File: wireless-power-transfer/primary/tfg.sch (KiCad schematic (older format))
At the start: 30 parts, among them J1 CONN_01X06, J2 Screw_Terminal_1x02, J3 BARREL_JACK, Q1 IRLB8721PBF, Q2 IRLB8721PBF, Q3 IRLB8721PBF, Q4 IRLB8721PBF, U1 PIC18F45K20-I/PT, U2 IR2110, U3 IR2110, U4 R-78E15, U5 R-78E3.3, U6 XBEE_Wi-Fi

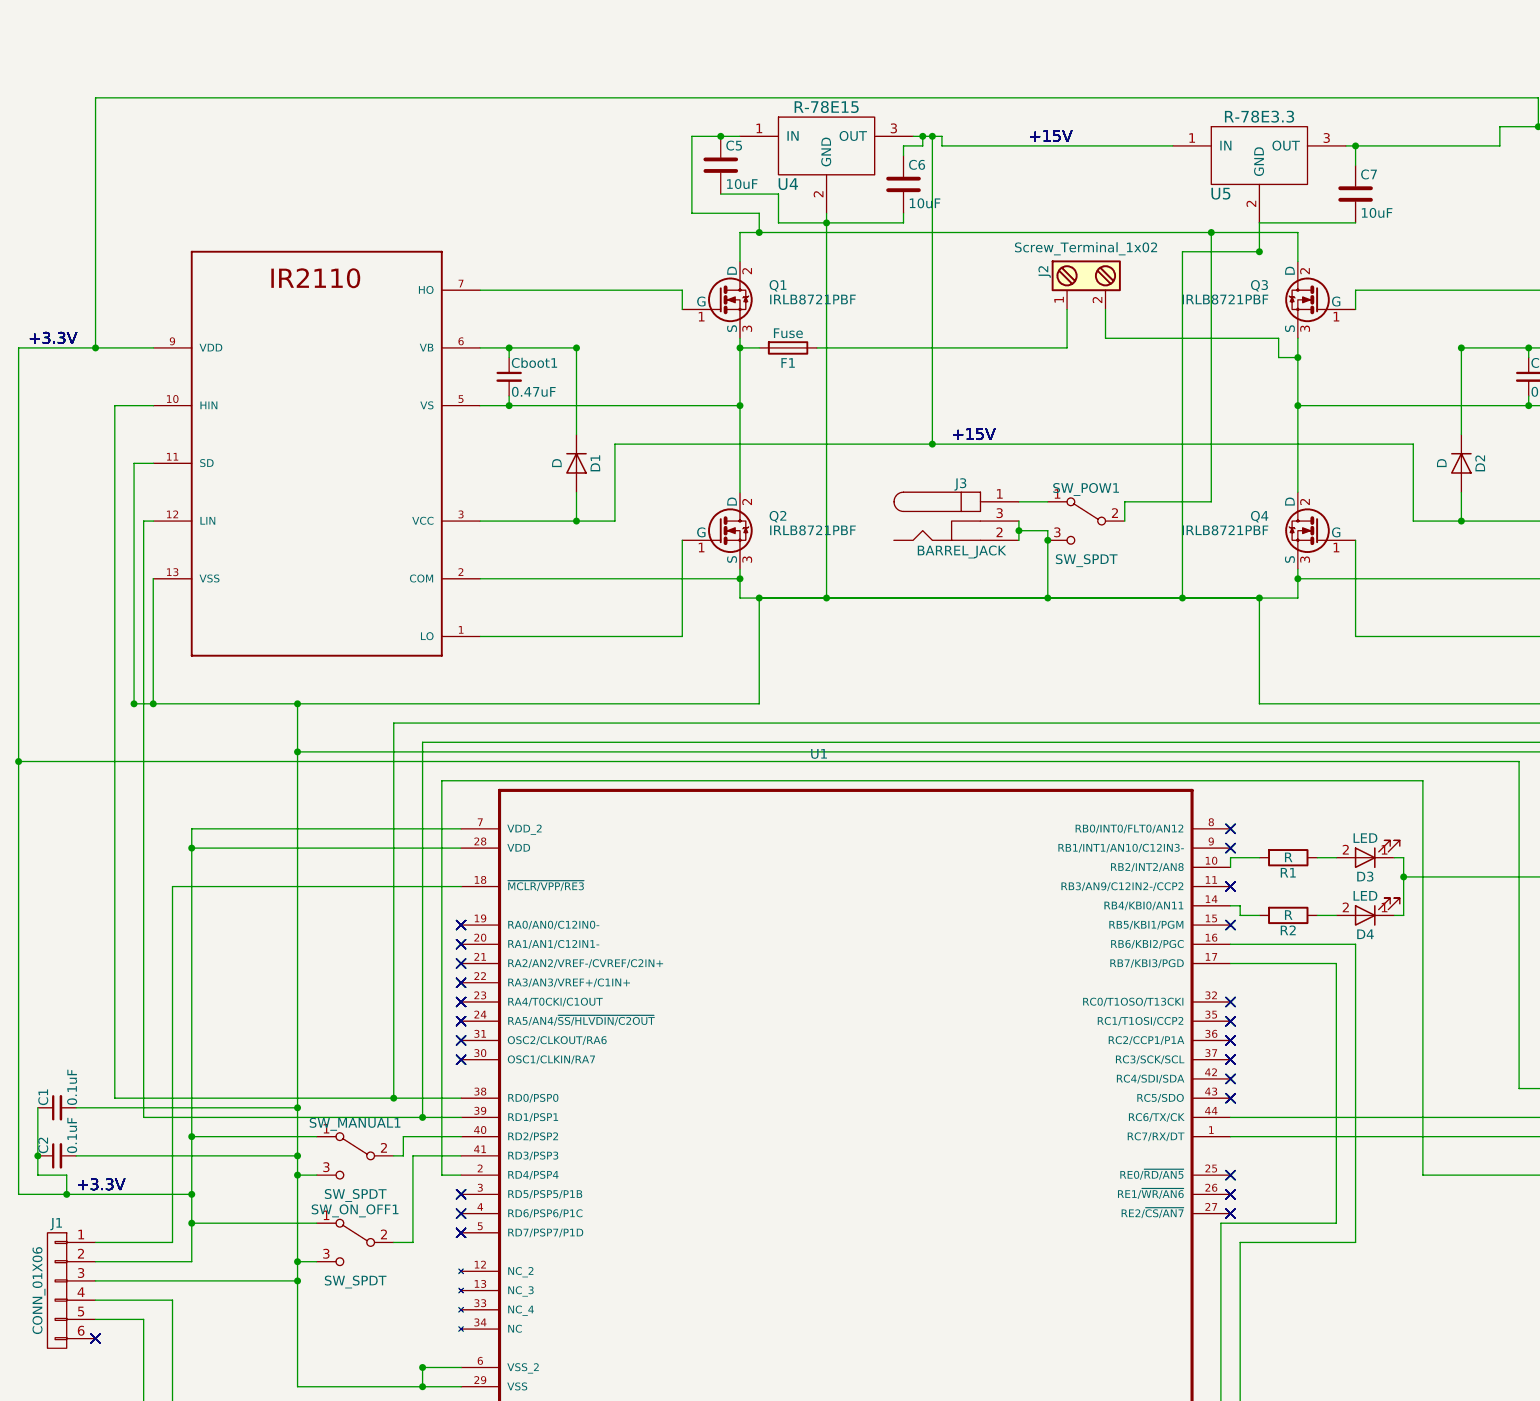
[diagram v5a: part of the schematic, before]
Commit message: Added resistor between pins 1 and 2 of the PicKit connector.
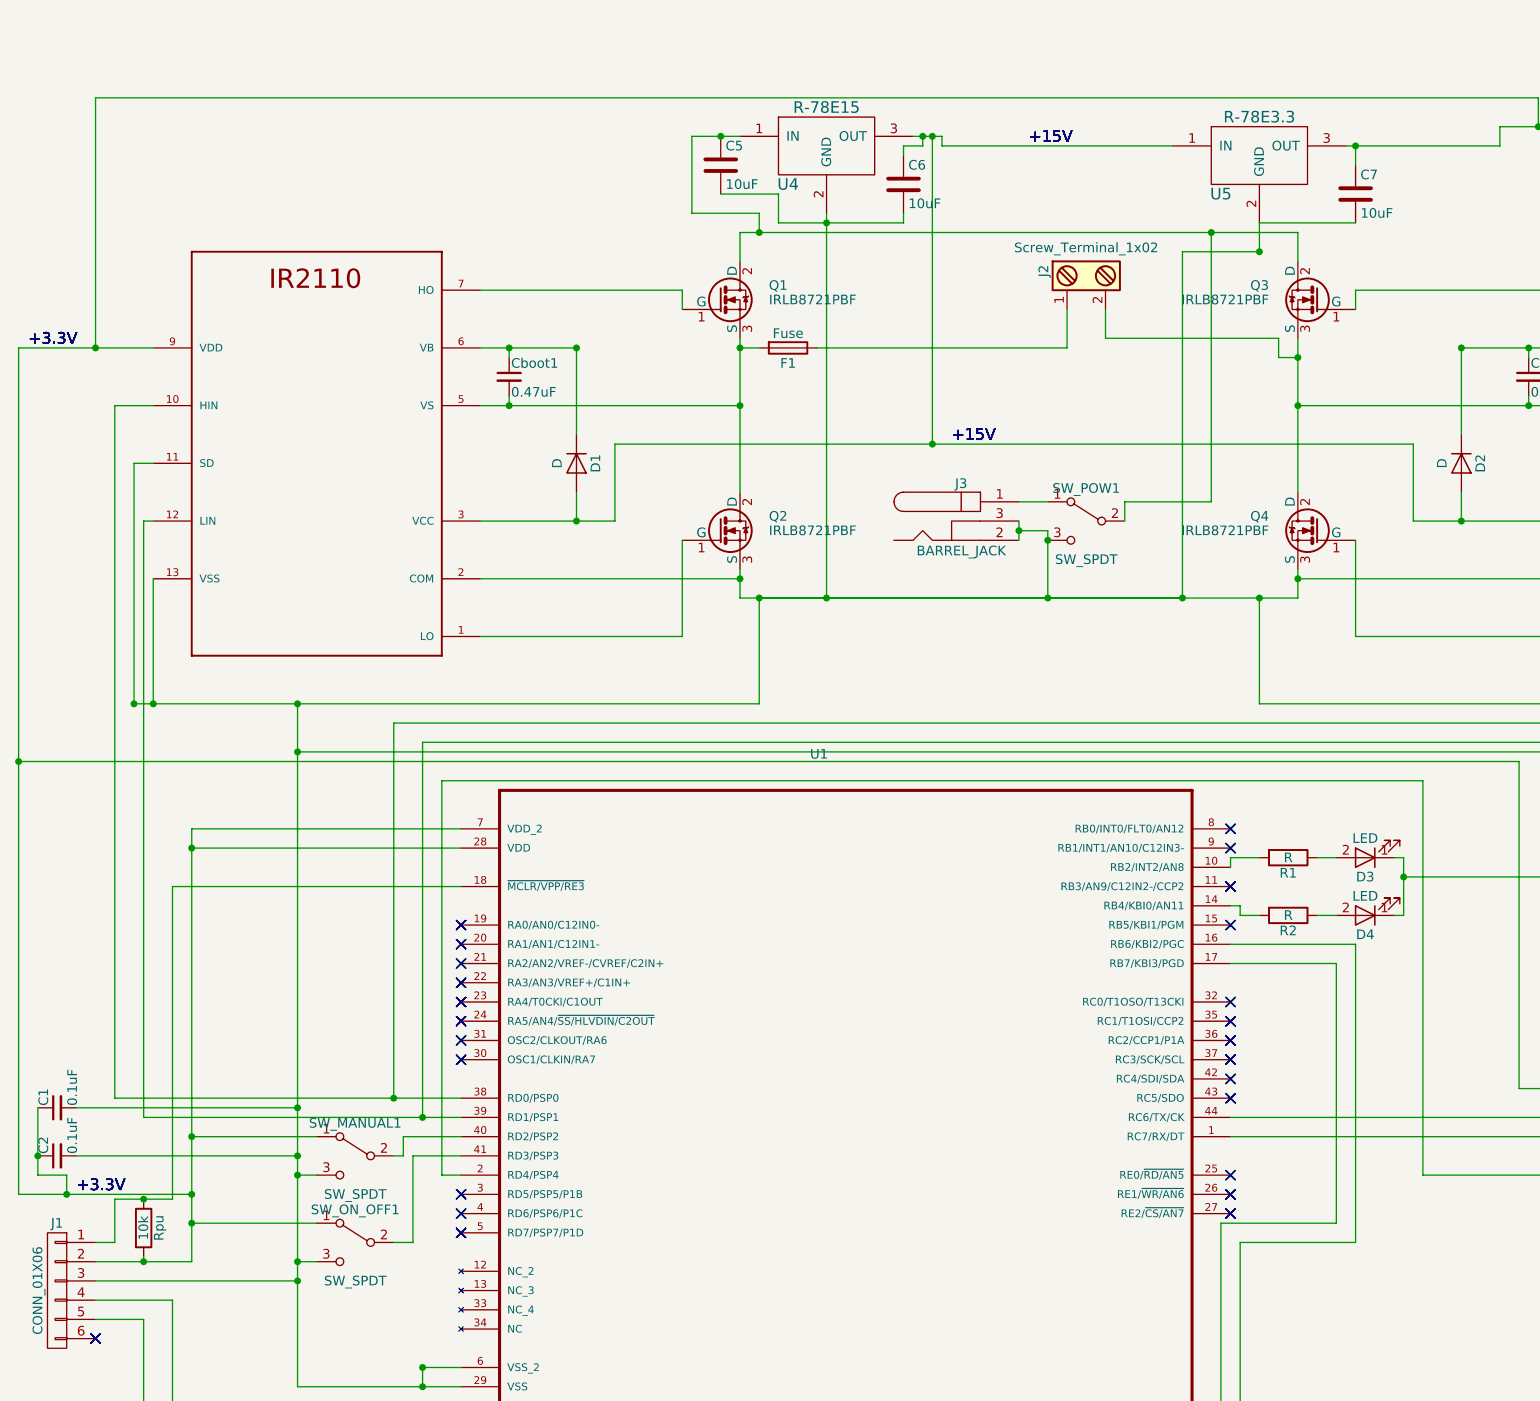
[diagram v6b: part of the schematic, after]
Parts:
- added Rpu: 10k, Resistors_SMD:R_1206_HandSoldering, symbol R
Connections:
- net +3.3V: now also Rpu.2
- net at J1.1 (P1), U1.18 (~MCLR/VPP/RE3): now also Rpu.1
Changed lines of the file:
@@
 Connection ~ 5750 7950
 Wire Wire Line
-	4050 7200 4450 7200
-Wire Wire Line
-	4450 7200 4450 5350
-Wire Wire Line
 	4450 5350 5950 5350
 Wire Wire Line
-	4050 7300 4550 7300
-Wire Wire Line
-	4550 7300 4550 5050
+	4550 5050 4550 7300
 Wire Wire Line
 	4550 5050 5950 5050
@@
 Connection ~ 7500 1950
 Wire Wire Line
-	9700 2050 9700 3850
+	9700 3850 9700 2050
 Connection ~ 9700 3850
 Wire Wire Line
@@
 	7500 1850 7500 1950
 Wire Wire Line
-	8450 1450 8300 1450
+	8300 1450 8450 1450
 Wire Wire Line
 	10100 1900 10100 2050
@@
 Connection ~ 13300 4400
 Wire Wire Line
-	7400 1450 7150 1450
+	7150 1450 7400 1450
 Wire Wire Line
 	7150 1450 7150 1850
@@
 	9400 3450 9400 3350
 Wire Wire Line
-	7500 3850 10100 3850
-Wire Wire Line
 	7400 3850 10300 3850
+Wire Wire Line
+	7500 3850 9700 3850
 Wire Wire Line
 	7850 1850 7850 3850
@@
 	10000 5450 10000 5500
 Wire Wire Line
-	10850 5500 10850 5200
+	10850 5200 10850 5500
 Wire Wire Line
 	10850 5300 11650 5300
@@
 	10850 5200 10800 5200
 Wire Wire Line
-	10800 5500 10850 5500
+	10850 5500 10800 5500
 Wire Wire Line
 	8400 3050 8400 1450
@@
 Wire Wire Line
 	9300 2350 9300 2500
+$Comp
+L R Rpu
+U 1 1 5A0EC076
+P 4300 7125
+F 0 "Rpu" V 4380 7125 50  0000 C CNN
+F 1 "10k" V 4300 7125 50  0000 C CNN
+F 2 "Resistors_SMD:R_1206_HandSoldering" V 4230 7125 50  0001 C CNN
+F 3 "" H 4300 7125 50  0001 C CNN
+	1    4300 7125
+	1    0    0    -1
+$EndComp
+Wire Wire Line
+	4550 7300 4050 7300
+Wire Wire Line
+	4300 7275 4300 7300
+Connection ~ 4300 7300
+Wire Wire Line
+	4150 6975 4450 6975
+Wire Wire Line
+	4150 6975 4150 7200
+Wire Wire Line
+	4150 7200 4050 7200
+Wire Wire Line
+	4450 6975 4450 5350
+Connection ~ 4300 6975
 $EndSCHEMATC

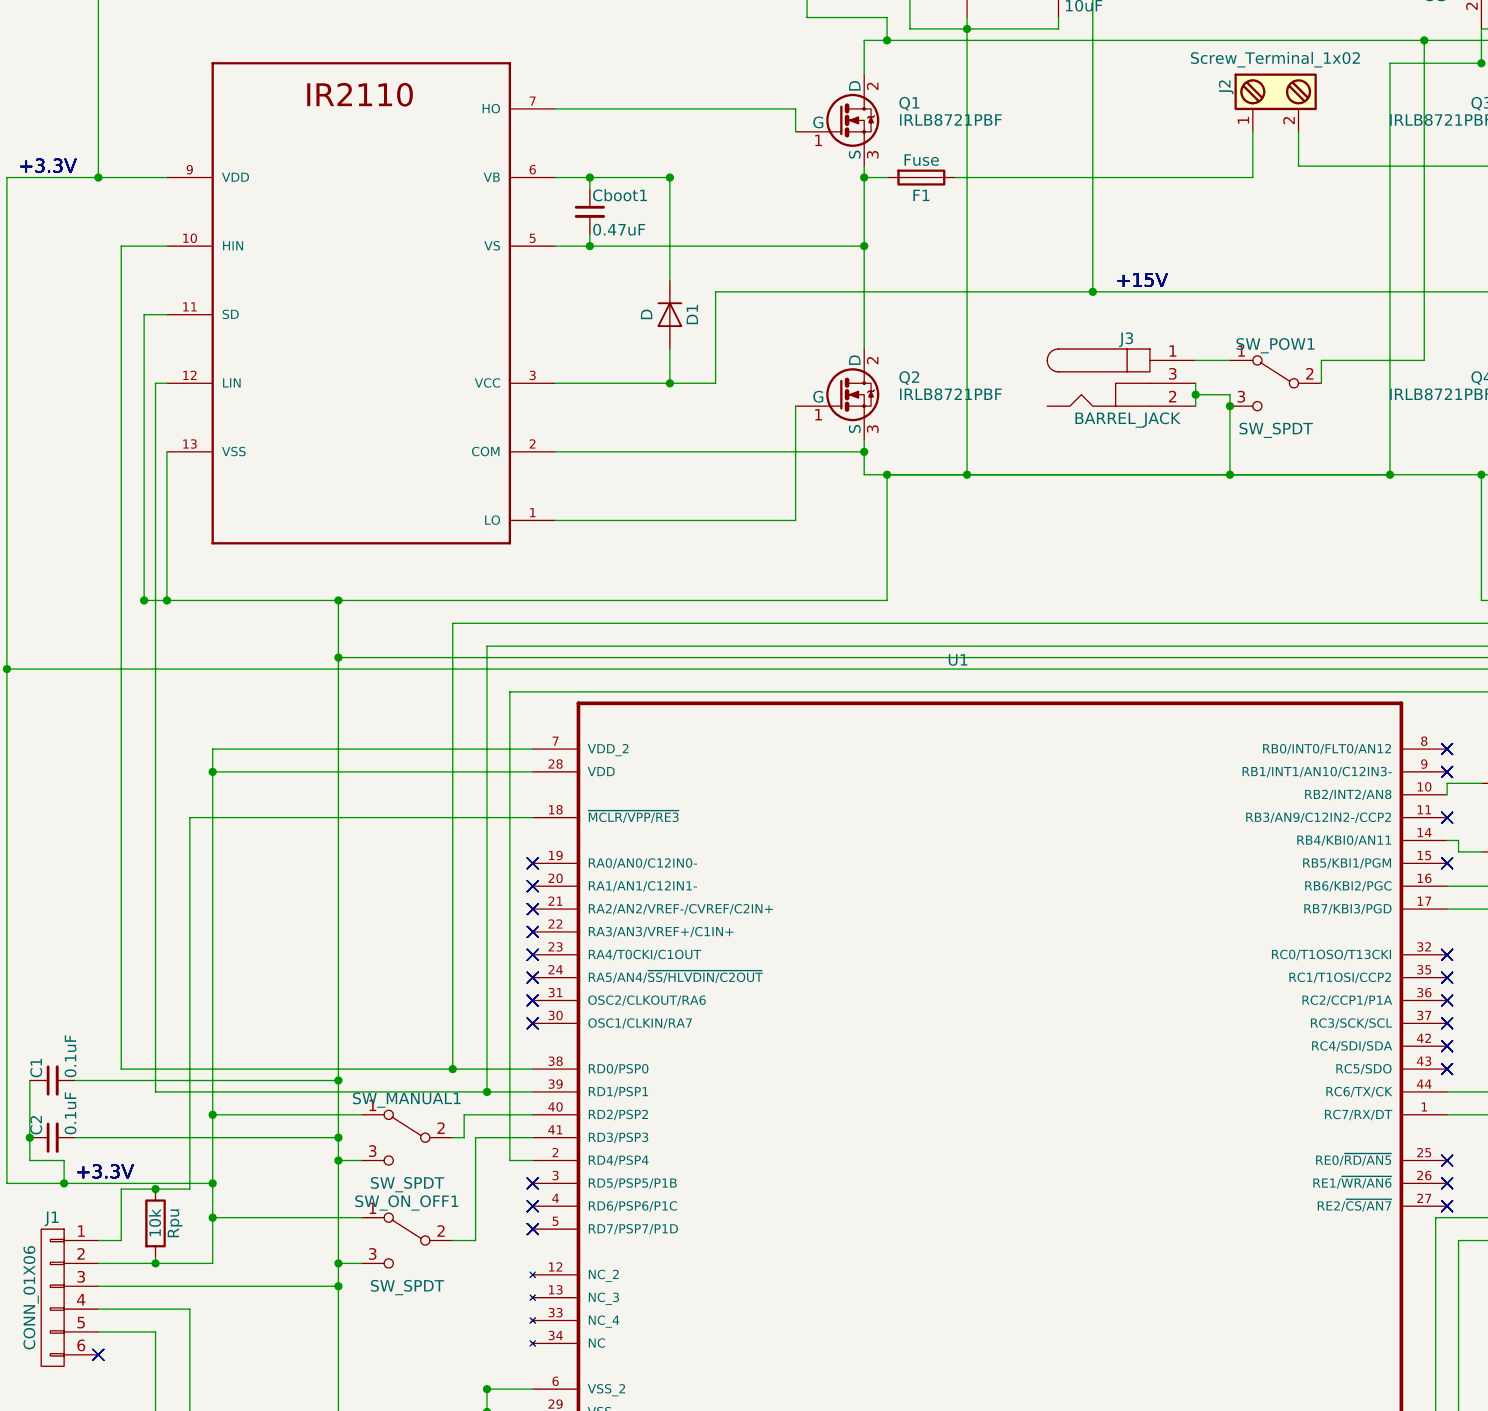
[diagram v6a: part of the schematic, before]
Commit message: The two PCBs of the primary circuit have been connected.
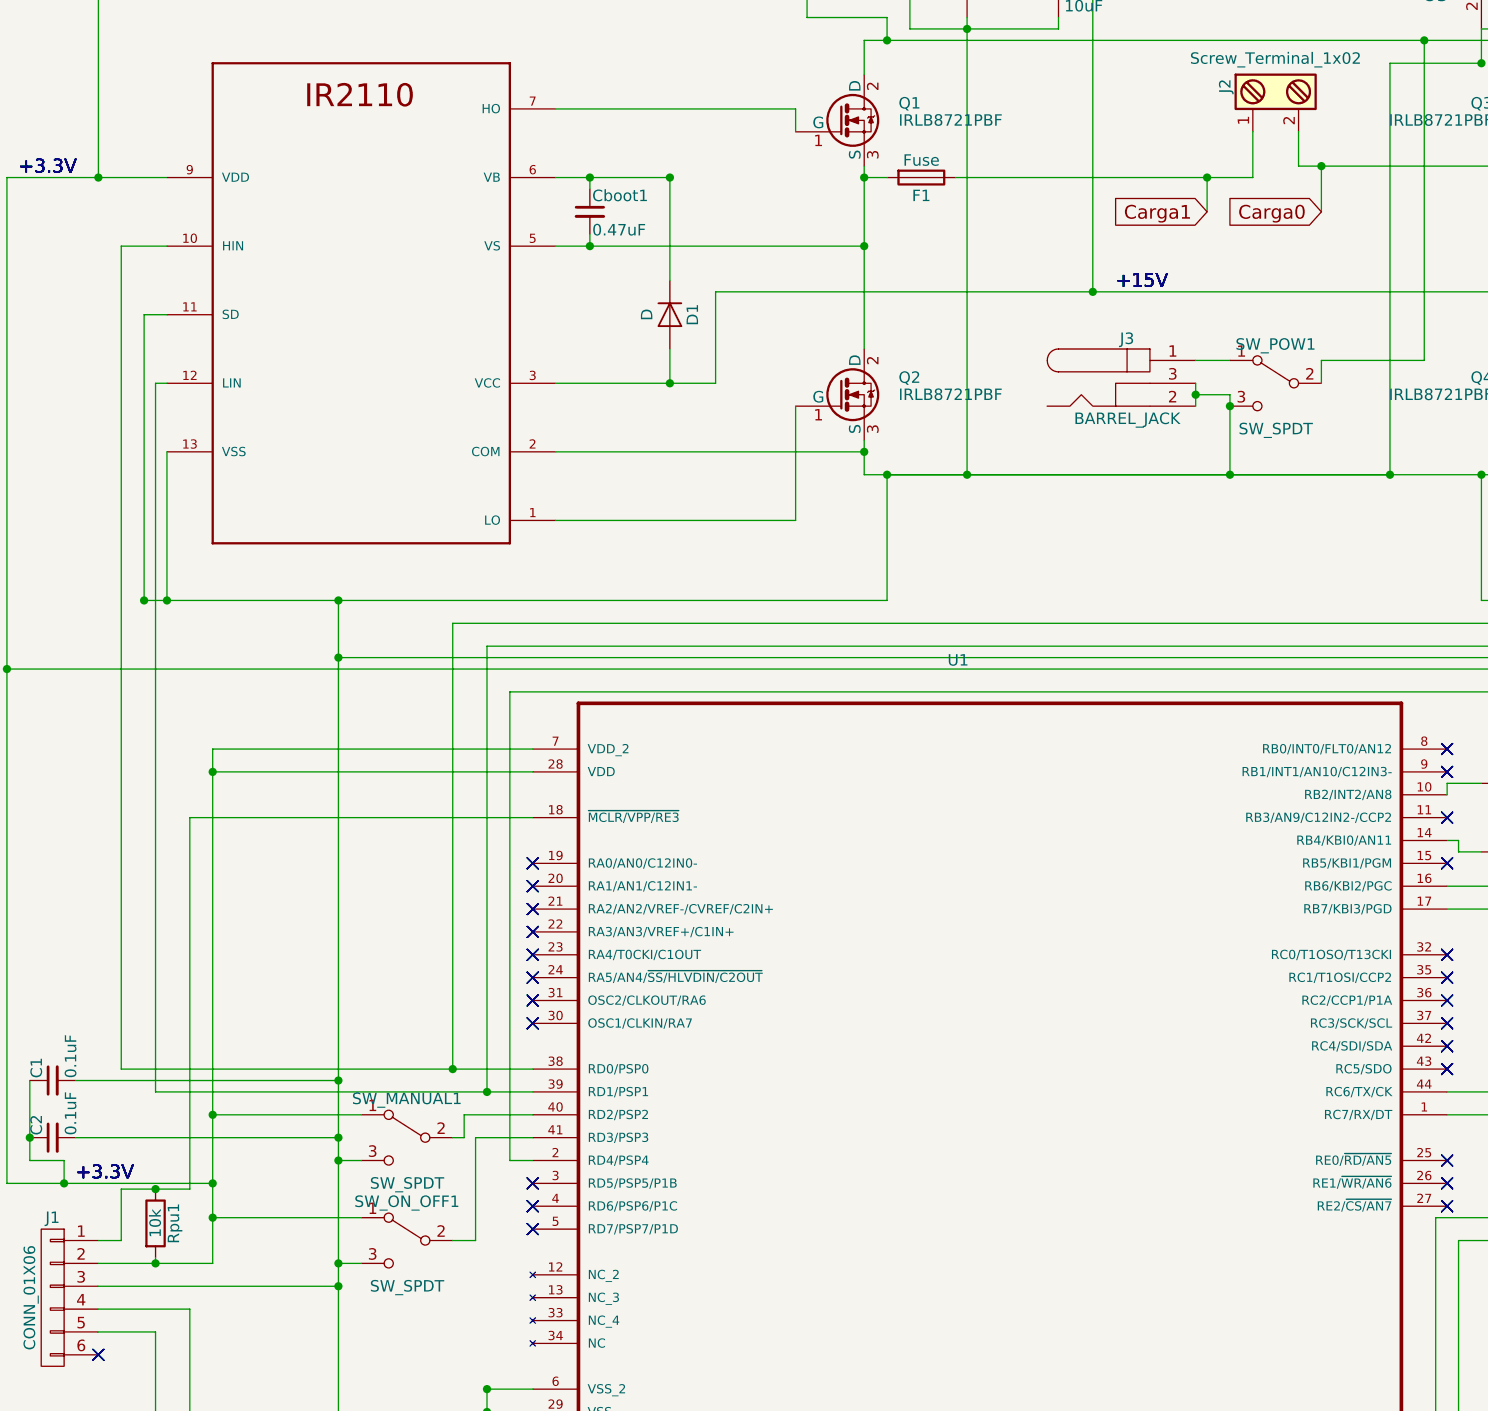
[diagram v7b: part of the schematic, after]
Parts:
- renumbered Rpu to Rpu1
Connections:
- net Carga0: now reaches Cboot2.2, J2.2, Q3.3 (S), Q4.2 (D), U3.5 (VS)
- net Carga1: now reaches F1.1, J2.1
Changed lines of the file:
@@
 LIBS:r-78exx
 LIBS:switches
-LIBS:xbee_wi-fi
 LIBS:irlb8721pbf
 LIBS:tfg-cache
@@
 	9300 2350 9300 2500
 $Comp
-L R Rpu
+L R Rpu1
 U 1 1 5A0EC076
 P 4300 7125
-F 0 "Rpu" V 4380 7125 50  0000 C CNN
+F 0 "Rpu1" V 4380 7125 50  0000 C CNN
 F 1 "10k" V 4300 7125 50  0000 C CNN
 F 2 "Resistors_SMD:R_1206_HandSoldering" V 4230 7125 50  0001 C CNN
@@
 	4450 6975 4450 5350
 Connection ~ 4300 6975
+Text GLabel 8900 2700 0    60   Input ~ 0
+Carga1
+Text GLabel 9400 2700 0    60   Input ~ 0
+Carga0
+Wire Wire Line
+	8900 2700 8900 2550
+Connection ~ 8900 2550
+Wire Wire Line
+	9400 2700 9400 2500
+Connection ~ 9400 2500
 $EndSCHEMATC

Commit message: PDFs created with schematics and PCB layers for front and back sides.
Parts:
- D3, D4: symbol LED -> LED-RESCUE-tfg
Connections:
- net at D3.2 (A): no longer R1.1
- net at D4.2 (A): no longer R2.1
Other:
- note added: "1/7"
- note removed: "1/3"
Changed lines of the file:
@@
 EESchema Schematic File Version 2
+LIBS:tfg-rescue
 LIBS:power
 LIBS:device
@@
 LIBS:r-78exx
 LIBS:switches
+LIBS:xbee_wi-fi
 LIBS:irlb8721pbf
 LIBS:tfg-cache
@@
 U 1 1 592C7ECA
 P 11500 2700
-F 0 "Cboot2" H 11510 2770 50  0000 L CNN
-F 1 "0.47uF" H 11510 2620 50  0000 L CNN
+F 0 "Cboot2" H 11225 2775 50  0000 L CNN
+F 1 "0.47uF" H 11225 2625 50  0000 L CNN
 F 2 "Capacitors_SMD:C_1206_HandSoldering" H 11500 2700 50  0001 C CNN
 F 3 "" H 11500 2700 50  0001 C CNN
@@
 NoConn ~ 11850 5350
 $Comp
-L LED D3
+L LED-RESCUE-tfg D3
 U 1 1 59E8E0C4
 P 10650 5200
@@
 $EndComp
 $Comp
-L LED D4
+L LED-RESCUE-tfg D4
 U 1 1 59E8E153
 P 10650 5500
@@
 	-1   0    0    -1
 $EndComp
-Text Notes 14950 11050 0    197  ~ 0
-1/3
+Text Notes 15100 11000 0    118  ~ 0
+1/7
 Text Label 8900 1500 0    60   ~ 0
 +15V
@@
 NoConn ~ 11950 5350
 NoConn ~ 11850 5350
-Text Notes 14950 11050 0    197  ~ 0
-1/3
 Text Label 8900 1500 0    60   ~ 0
 +15V
@@
 NoConn ~ 11950 5350
 NoConn ~ 11850 5350
-Text Notes 14950 11050 0    197  ~ 0
-1/3
 Text Label 8900 1500 0    60   ~ 0
 +15V
@@
 NoConn ~ 11950 5350
 NoConn ~ 11850 5350
-Text Notes 14950 11050 0    197  ~ 0
-1/3
 $Sheet
 S 16950 0    8050 11650
